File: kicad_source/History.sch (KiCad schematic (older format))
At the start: 0 parts

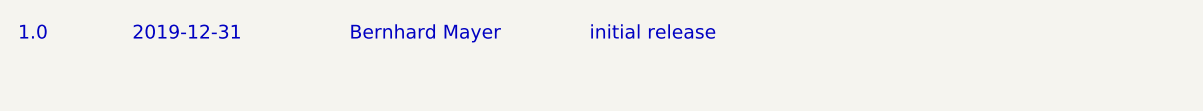
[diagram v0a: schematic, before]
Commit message: added external supply for +5V for TMC5130
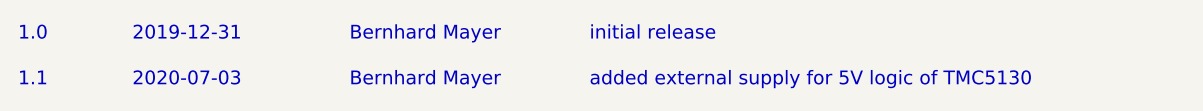
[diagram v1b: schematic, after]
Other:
- note added: "1.1"
- note added: "2020-07-03"
- note added: "added external supply for 5V logic of TMC5130"
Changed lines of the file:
@@
 Text Notes 3350 900  0    60   ~ 0
 initial release
+Text Notes 850  1100 0    60   ~ 0
+1.1
+Text Notes 1350 1100 0    60   ~ 0
+2020-07-03
+Text Notes 2300 1100 0    60   ~ 0
+Bernhard Mayer
+Text Notes 3350 1100 0    60   ~ 0
+added external supply for 5V logic of TMC5130
 $EndSCHEMATC

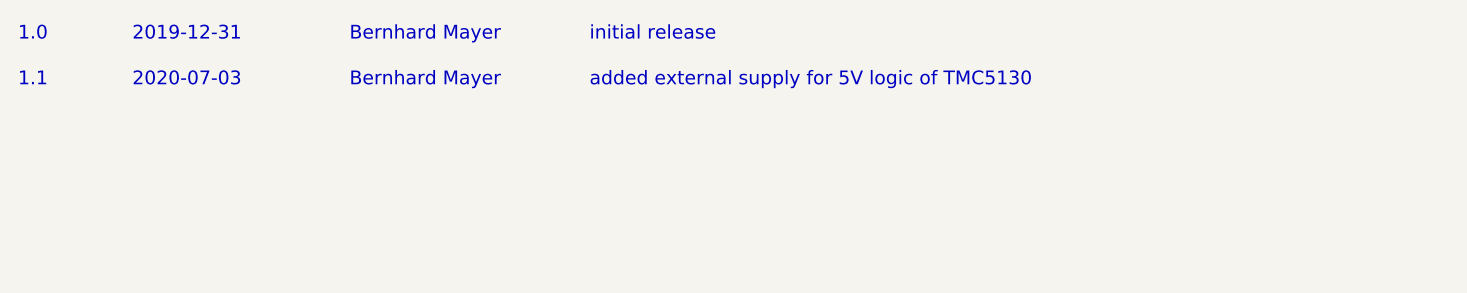
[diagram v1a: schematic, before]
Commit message: added clock generator as common clock for both stepper drivers
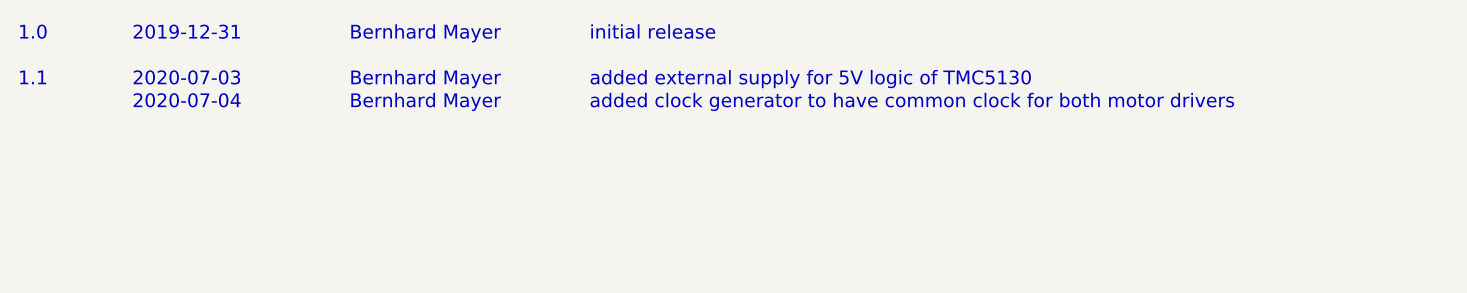
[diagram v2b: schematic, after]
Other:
- note added: "2020-07-04"
- note added: "added clock generator to have common clock for both motor drivers"
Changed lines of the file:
@@
 $Descr A4 11693 8268
 encoding utf-8
-Sheet 4 6
+Sheet 6 6
 Title "HighPowerMotorFeatherWing"
 Date "2019-12-31"
@@
 Text Notes 3350 1100 0    60   ~ 0
 added external supply for 5V logic of TMC5130
+Text Notes 1350 1200 0    60   ~ 0
+2020-07-04
+Text Notes 2300 1200 0    60   ~ 0
+Bernhard Mayer
+Text Notes 3350 1200 0    60   ~ 0
+added clock generator to have common clock for both motor drivers
 $EndSCHEMATC

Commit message: added leds and decoupling capacitors
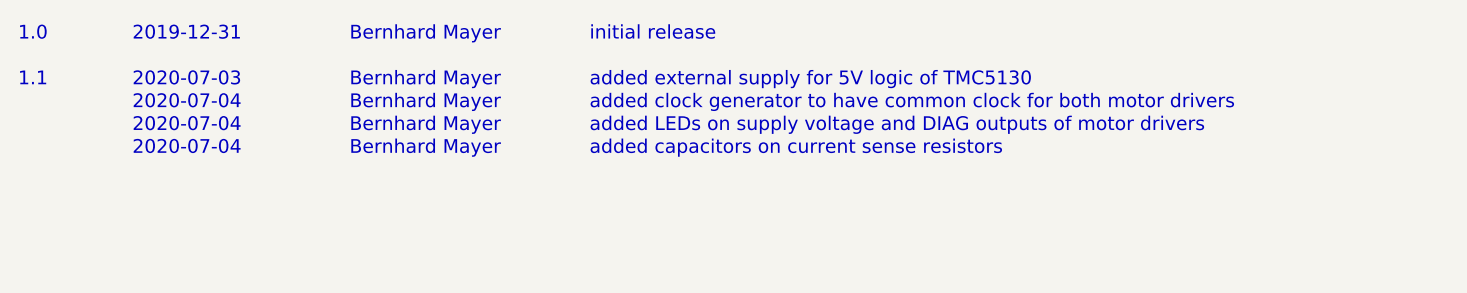
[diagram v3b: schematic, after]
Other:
- note added: "added LEDs on supply voltage and DIAG outputs of motor drivers"
- note added: "added capacitors on current sense resistors"
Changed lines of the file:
@@
 Sheet 6 6
 Title "HighPowerMotorFeatherWing"
-Date "2019-12-31"
-Rev "1.0"
+Date "2020-07-04"
+Rev "1.1"
 Comp "generationmake"
 Comment1 ""
@@
 Text Notes 3350 1200 0    60   ~ 0
 added clock generator to have common clock for both motor drivers
+Text Notes 1350 1300 0    60   ~ 0
+2020-07-04
+Text Notes 2300 1300 0    60   ~ 0
+Bernhard Mayer
+Text Notes 3350 1300 0    60   ~ 0
+added LEDs on supply voltage and DIAG outputs of motor drivers
+Text Notes 1350 1400 0    60   ~ 0
+2020-07-04
+Text Notes 2300 1400 0    60   ~ 0
+Bernhard Mayer
+Text Notes 3350 1400 0    60   ~ 0
+added capacitors on current sense resistors
 $EndSCHEMATC

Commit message: added temperature sensor LM75
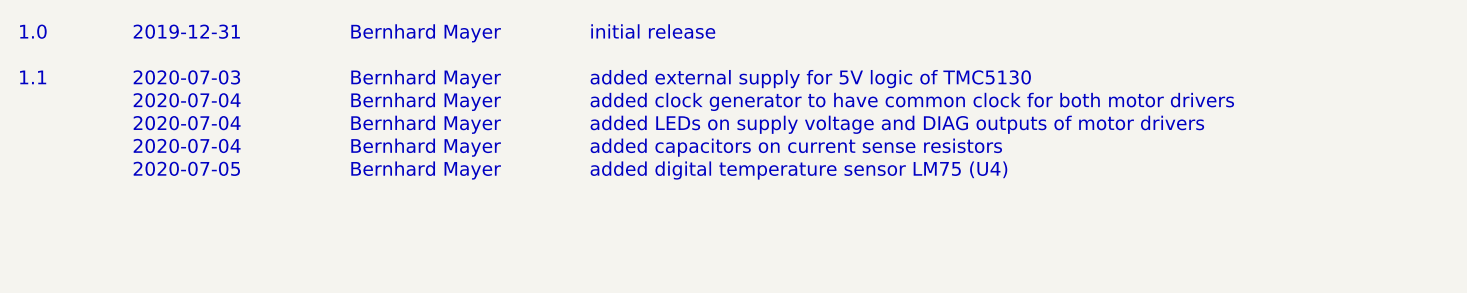
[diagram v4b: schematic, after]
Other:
- note added: "2020-07-05"
- note added: "added digital temperature sensor LM75 (U4)"
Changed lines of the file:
@@
 Text Notes 3350 1400 0    60   ~ 0
 added capacitors on current sense resistors
+Text Notes 1350 1500 0    60   ~ 0
+2020-07-05
+Text Notes 2300 1500 0    60   ~ 0
+Bernhard Mayer
+Text Notes 3350 1500 0    60   ~ 0
+added digital temperature sensor LM75 (U4)
 $EndSCHEMATC

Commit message: updated layout
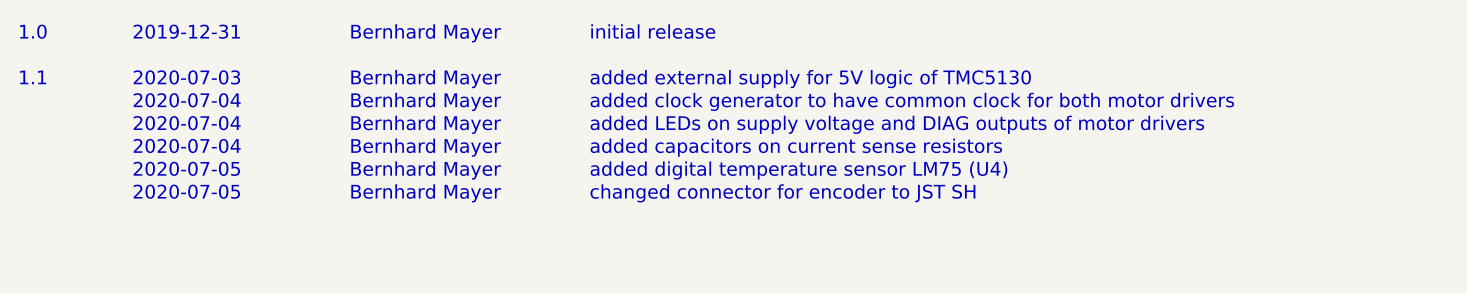
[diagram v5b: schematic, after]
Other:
- note added: "changed connector for encoder to JST SH"
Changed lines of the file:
@@
 Text Notes 3350 1500 0    60   ~ 0
 added digital temperature sensor LM75 (U4)
+Text Notes 1350 1600 0    60   ~ 0
+2020-07-05
+Text Notes 2300 1600 0    60   ~ 0
+Bernhard Mayer
+Text Notes 3350 1600 0    60   ~ 0
+changed connector for encoder to JST SH
 $EndSCHEMATC

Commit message: added expansion connector, updated layout
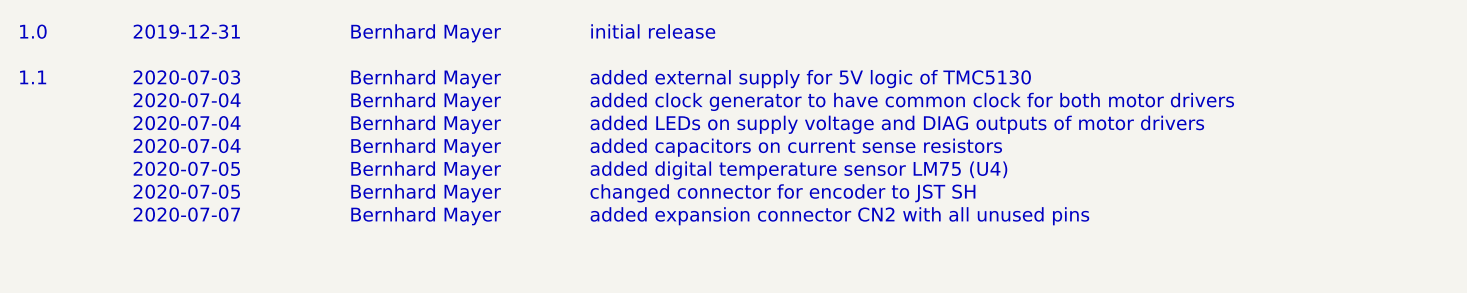
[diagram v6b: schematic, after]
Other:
- note added: "2020-07-07"
- note added: "added expansion connector CN2 with all unused pins"
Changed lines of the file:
@@
 Sheet 6 6
 Title "HighPowerMotorFeatherWing"
-Date "2020-07-04"
+Date "2020-07-08"
 Rev "1.1"
 Comp "generationmake"
@@
 Text Notes 3350 1600 0    60   ~ 0
 changed connector for encoder to JST SH
+Text Notes 1350 1700 0    60   ~ 0
+2020-07-07
+Text Notes 2300 1700 0    60   ~ 0
+Bernhard Mayer
+Text Notes 3350 1700 0    60   ~ 0
+added expansion connector CN2 with all unused pins
 $EndSCHEMATC

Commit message: corrected position of mounting holes for heat spreader, added information on input voltage
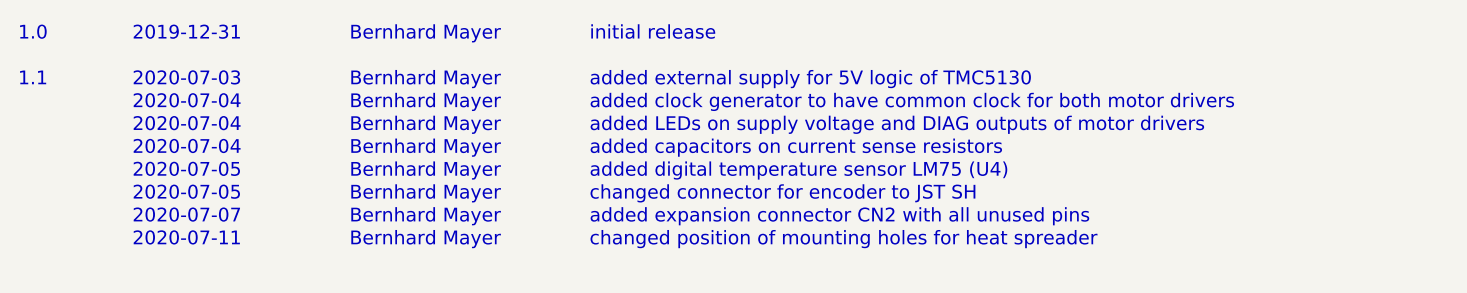
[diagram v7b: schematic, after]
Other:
- note added: "2020-07-11"
- note added: "changed position of mounting holes for heat spreader"
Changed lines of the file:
@@
 Text Notes 3350 1700 0    60   ~ 0
 added expansion connector CN2 with all unused pins
+Text Notes 1350 1800 0    60   ~ 0
+2020-07-11
+Text Notes 2300 1800 0    60   ~ 0
+Bernhard Mayer
+Text Notes 3350 1800 0    60   ~ 0
+changed position of mounting holes for heat spreader
 $EndSCHEMATC

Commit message: changed L1 and L2 to Sumida 0624CDMCCDS for better availability
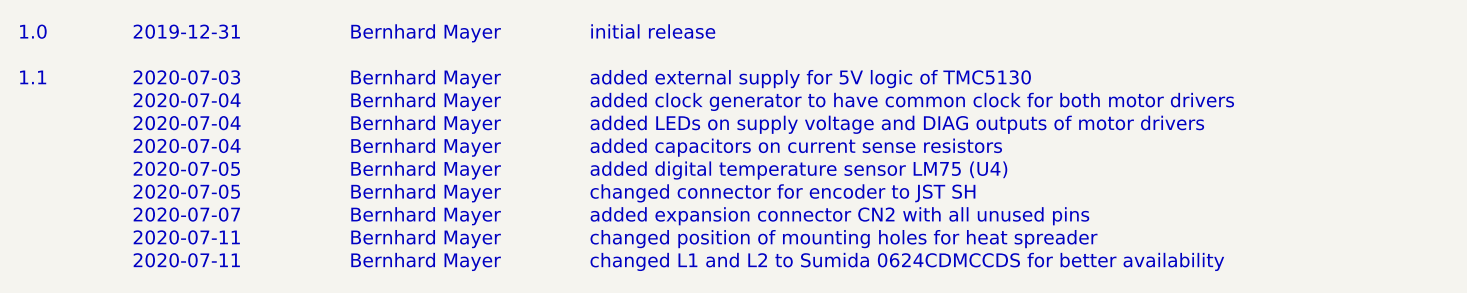
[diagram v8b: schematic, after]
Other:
- note added: "changed L1 and L2 to Sumida 0624CDMCCDS for better availability"
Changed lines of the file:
@@
 Text Notes 3350 1800 0    60   ~ 0
 changed position of mounting holes for heat spreader
+Text Notes 1350 1900 0    60   ~ 0
+2020-07-11
+Text Notes 2300 1900 0    60   ~ 0
+Bernhard Mayer
+Text Notes 3350 1900 0    60   ~ 0
+changed L1 and L2 to Sumida 0624CDMCCDS for better availability
 $EndSCHEMATC
